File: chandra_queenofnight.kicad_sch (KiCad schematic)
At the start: 0 parts

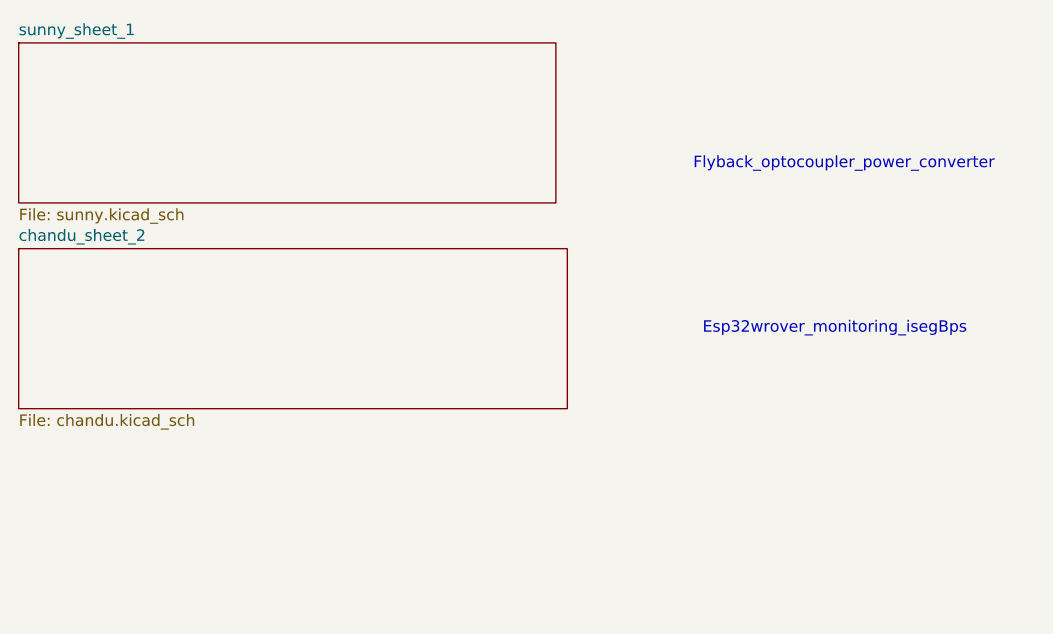
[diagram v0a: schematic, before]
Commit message: Initialtes gndplane
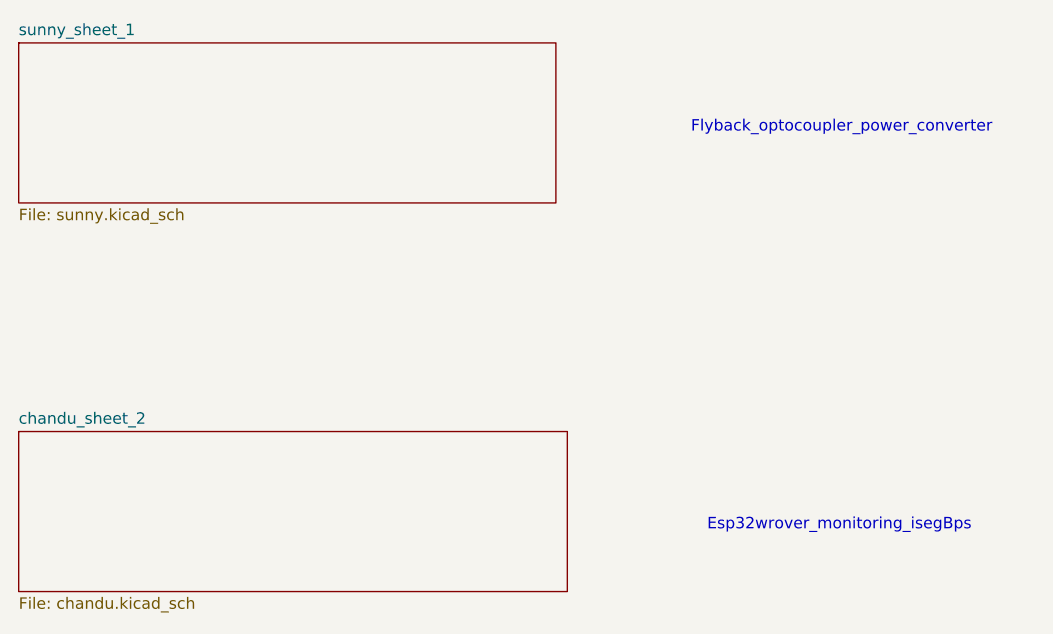
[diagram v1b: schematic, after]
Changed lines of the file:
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@@
 	(text "Flyback_optocoupler_power_converter"
 		(exclude_from_sim no)
-		(at 109.474 28.702 0)
+		(at 109.22 24.638 0)
 		(effects
 			(font
@@
 	(text "Esp32wrover_monitoring_isegBps"
 		(exclude_from_sim no)
-		(at 108.458 46.99 0)
+		(at 108.966 68.834 0)
 		(effects
 			(font
@@
 	)
 	(sheet
-		(at 17.78 38.1)
+		(at 17.78 58.42)
 		(size 60.96 17.78)
 		(exclude_from_sim no)
@@
 		)
 		(property "Sheetname" "chandu_sheet_2"
-			(at 17.78 37.3884 0)
+			(at 17.78 57.7084 0)
 			(show_name no)
 			(do_not_autoplace no)
@@
 		)
 		(property "Sheetfile" "chandu.kicad_sch"
-			(at 17.78 56.4646 0)
+			(at 17.78 76.7846 0)
 			(show_name no)
 			(do_not_autoplace no)
